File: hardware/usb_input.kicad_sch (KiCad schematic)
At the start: 53 parts, among them J100 USB_C_Receptacle_USB2.0, J101 Conn_01x02_Male, Q100 DMP3036SSD, Q101 ???, U100 CYPD3177, U101 T2N7002AK

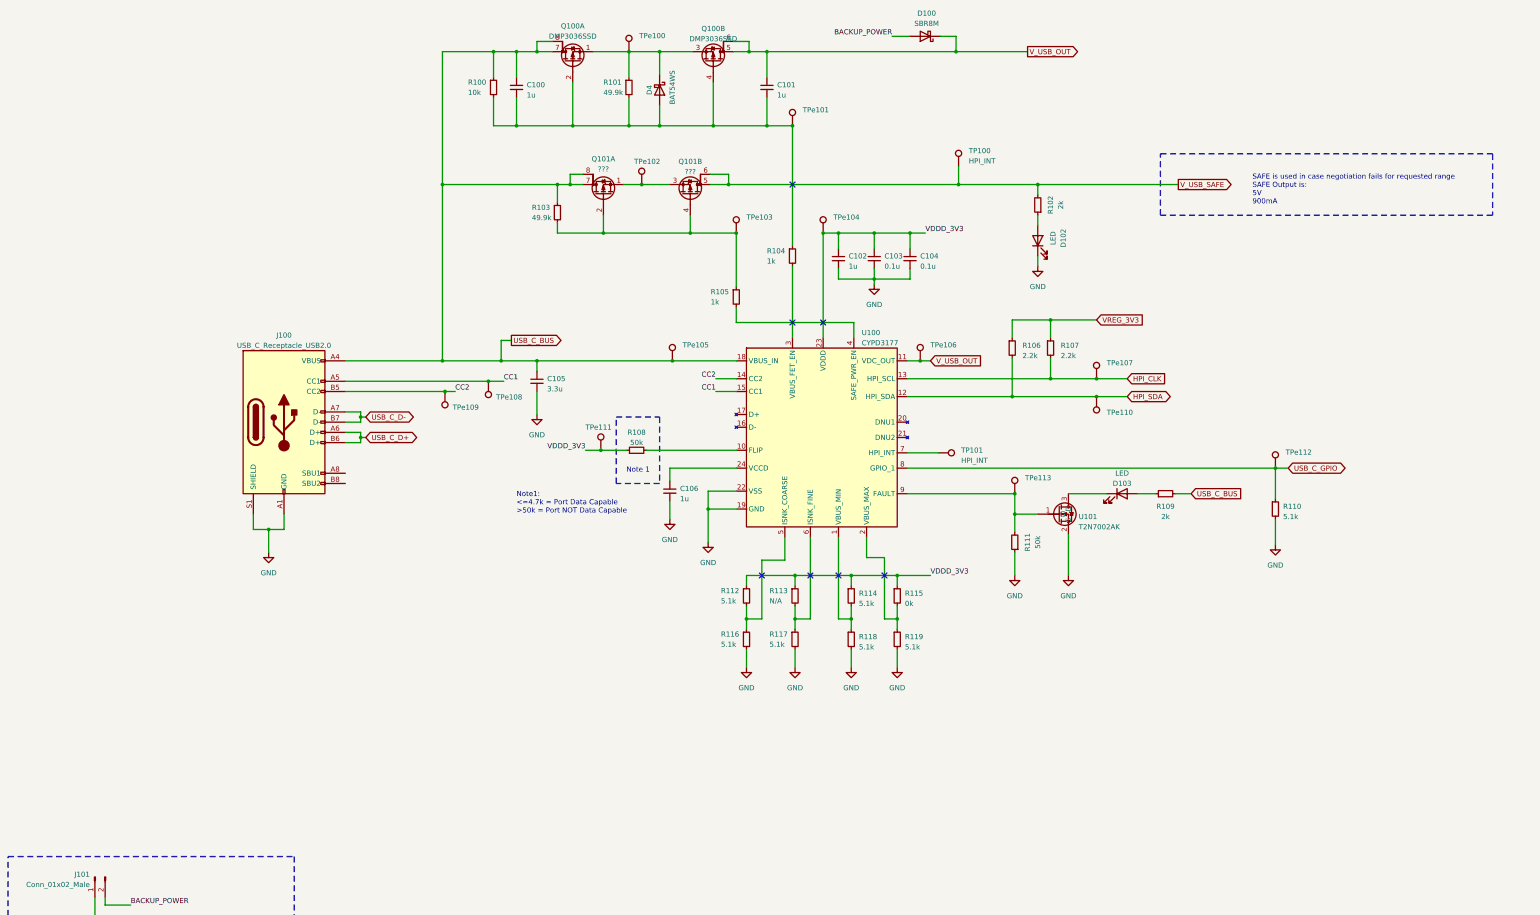
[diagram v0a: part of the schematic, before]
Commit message: Component values chosen for bat. charge, bat. protect, USB input
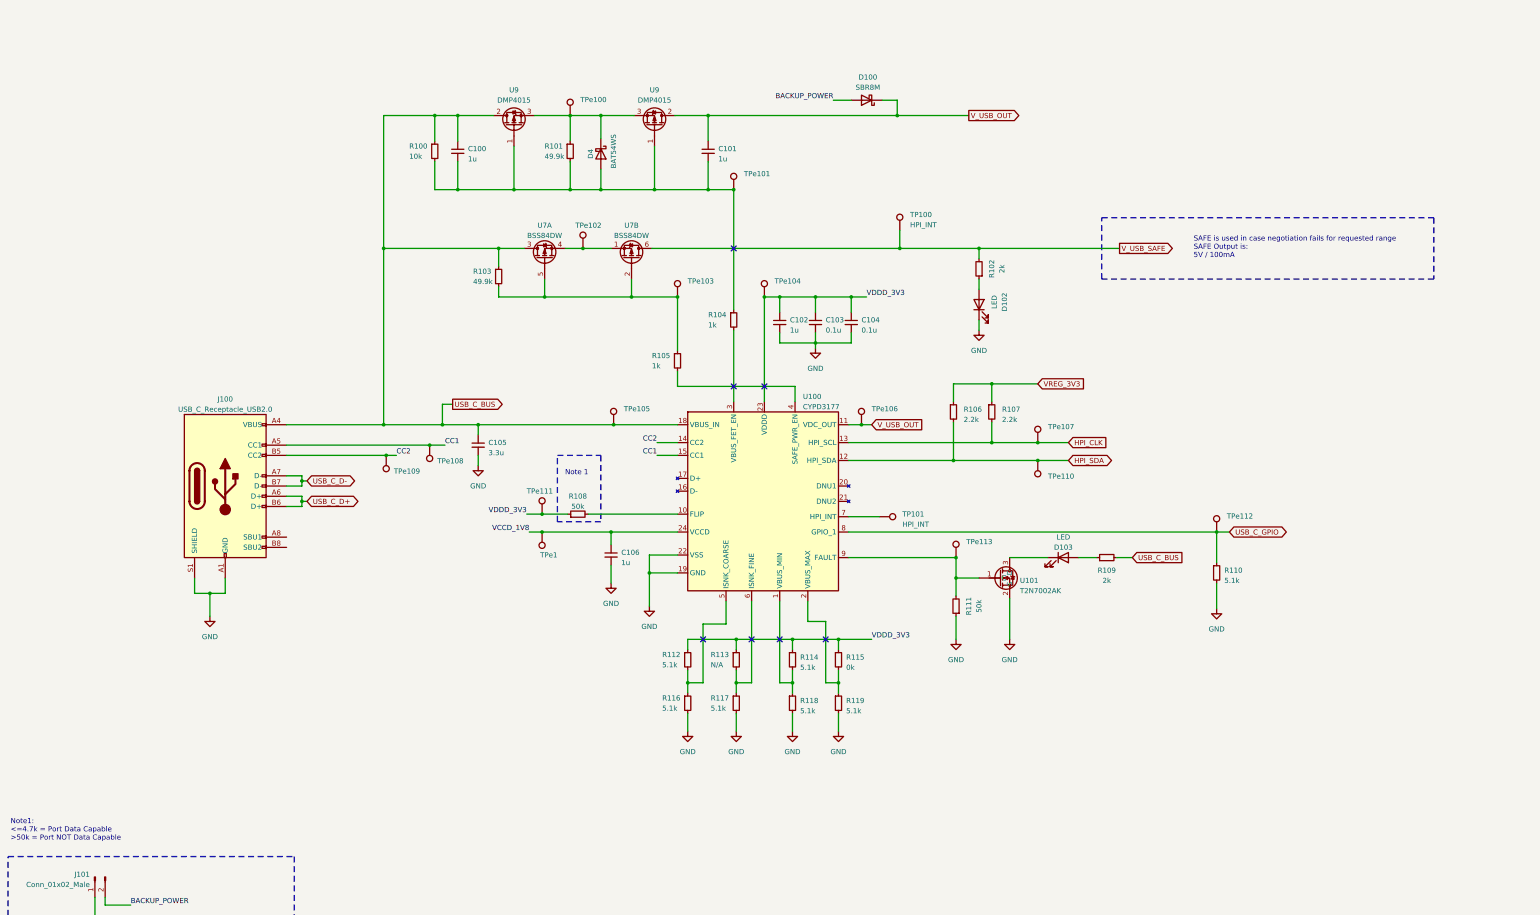
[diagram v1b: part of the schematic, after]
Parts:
- removed Q100: DMP3036SSD, Package_SO:SO-8_3.9x4.9mm_P1.27mm, symbol Device:Q_Dual_PMOS_S1G1S2G2D2D2D1D1
- removed Q101: ???, Package_SO:SO-8_3.9x4.9mm_P1.27mm, symbol Device:Q_Dual_PMOS_S1G1S2G2D2D2D1D1
- added TPe1: TestPoint, TestPoint:TestPoint_Pad_D1.0mm, symbol Connector:TestPoint
- added U7: BSS84DW, Package_TO_SOT_SMD:SOT-363_SC-70-6, symbol User_MOSFET:DSS84DW
- added U9 (x2): DMP4015, Package_TO_SOT_SMD:TO-252-2, symbol User_MOSFET:DMP4015
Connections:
- net USB_C_BUS: now also U7.3, U9.2
- net V_USB_OUT: now also U9.2
- net V_USB_SAFE: now also U7.6
- net VCCD_1V8: now reaches C106.1, U100.24 (VCCD)
- net VCCD_1V8: now also TPe1.1
- net at TPe102.1: now also U7.1, U7.4
- net at R103.2, R105.1, TPe103.1: now also U7.2, U7.5
- net at C100.2, C101.2, D4.2 (A)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: now also U9.1, U9.1
- net at D4.1 (K), R101.1, TPe100.1: now also U9.3, U9.3
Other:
- note added: "SAFE is used in case negotiation fails for requested range SAFE Output is: 5V / 100mA"
- note removed: "SAFE is used in case negotiation fails for requested range SAFE Output is: 5V 900mA"
- moved on the sheet: C100, C101, C102, C103, C104, C105, C106, D100, D102, D103, D4, J100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

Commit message: More simulation and work done on SEPIC stage. MOSFET changes to USB stage and charging stage.
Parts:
- removed U100: CYPD3177, Package_DFN_QFN:QFN-24-1EP_4x4mm_P0.5mm_EP2.65x2.65mm, symbol User_USB_C_PD:CYPD3177
- removed U9 (x2): DMP4015, Package_TO_SOT_SMD:TO-252-2, symbol User_MOSFET:DMP4015
- added J1: USB_C_Receptacle_USB2.0, Connector_USB:USB_C_Receptacle_GCT_USB4085, symbol Connector:USB_C_Receptacle_USB2.0
- added Q7: SQJ951EP, Daniel_xMOS:PowerPAK® SO-8L Dual, symbol Daniel_PMOS:Q_Dual_PMOS_S1G1S2G2D2D1
- added U11: CYPD3177, Package_DFN_QFN:QFN-24-1EP_4x4mm_P0.5mm_EP2.75x2.75mm, symbol Daniel_USB:CYPD3177
- R108: value 50k -> 60k
- R113: value N/A -> 5.1k
- R116, R118: value 5.1k -> 10k
- R119: value 5.1k -> N/A
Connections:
- net CC1: now also U11.15 (CC1)
- net CC2: now also U11.14 (CC2)
- net GND: now also J1.A1 (GND), J1.A12 (GND), J1.B1 (GND), J1.B12 (GND), J1.S1 (SHIELD), U11.19 (GND), U11.22 (VSS)
- net HPI_SDA: now also U11.12 (HPI_SDA)
- net USB_C_BUS: now also Q7.6, U11.18 (VBUS_IN)
- net USB_C_D+: now also J1.A6 (D+), J1.B6 (D+); no longer J100.A6 (D+), J100.B6 (D+)
- net USB_C_D-: now also J1.A7 (D-), J1.B7 (D-); no longer J100.A7 (D-), J100.B7 (D-)
- net USB_C_GPIO: now also U11.8 (GPIO_1)
- net VCCD_1V8: now also U11.24 (VCCD)
- net V_USB_OUT: now also Q7.5, U11.11 (VDC_OUT)
- net at R112.2, R116.1: now also U11.5 (ISNK_COARSE)
- net at R115.2, R119.1: now also U11.2 (VBUS_MAX)
- net at R111.2, TPe113.1, U101.1: now also U11.9 (FAULT)
- net at R114.2, R118.1: now also U11.1 (VBUS_MIN)
- net at R108.2: now also U11.10 (FLIP)
- net at R113.2, R117.1: now also U11.6 (ISNK_FINE)
- net at TP101.1: now also U11.7 (HPI_INT)
- net at C100.2, C101.2, D4.2 (A)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: now also Q7.2, Q7.4
- net at D4.1 (K), R101.1, TPe100.1: now also Q7.1, Q7.3
- net HPI_CLK renamed HPI_SCL
- net HPI_SCL: now also U11.13 (HPI_SCL)
- new net: J1.A4 (VBUS), J1.A9 (VBUS), J1.B4 (VBUS), J1.B9 (VBUS)
- no-connect marks 7 -> 13
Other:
- note added: "19V"
- note added: "20V"
- note added: "4A"
- note added: "750mA"
- moved on the sheet: C100, C101, C102, C103, C104, C105, C106, D100, D102, D103, D4, J100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

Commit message: Saving prior to changing project structure
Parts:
- removed R106, R107: 2.2k, Resistor_SMD:R_0805_2012Metric_Pad1.20x1.40mm_HandSolder, symbol Device:R_Small
- D100: value SBR8M -> SS16FP; footprint Diode_SMD:D_PowerDI-5 -> Diode_SMD:D_SOD-123; Cost 0.48 -> (none); Vendor https://www.mouser.com/ProductDetail/Diodes-Incorporated/SB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 -> (none)
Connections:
- net BACKUP_POWER: no longer D100.2 (A)
- net USB_C_COM_POWER: now reaches J1.A4 (VBUS), J1.A9 (VBUS), J1.B4 (VBUS), J1.B9 (VBUS)
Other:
- moved on the sheet: TPe107, TPe110
